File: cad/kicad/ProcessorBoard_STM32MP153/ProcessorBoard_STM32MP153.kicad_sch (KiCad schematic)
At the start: 4 parts

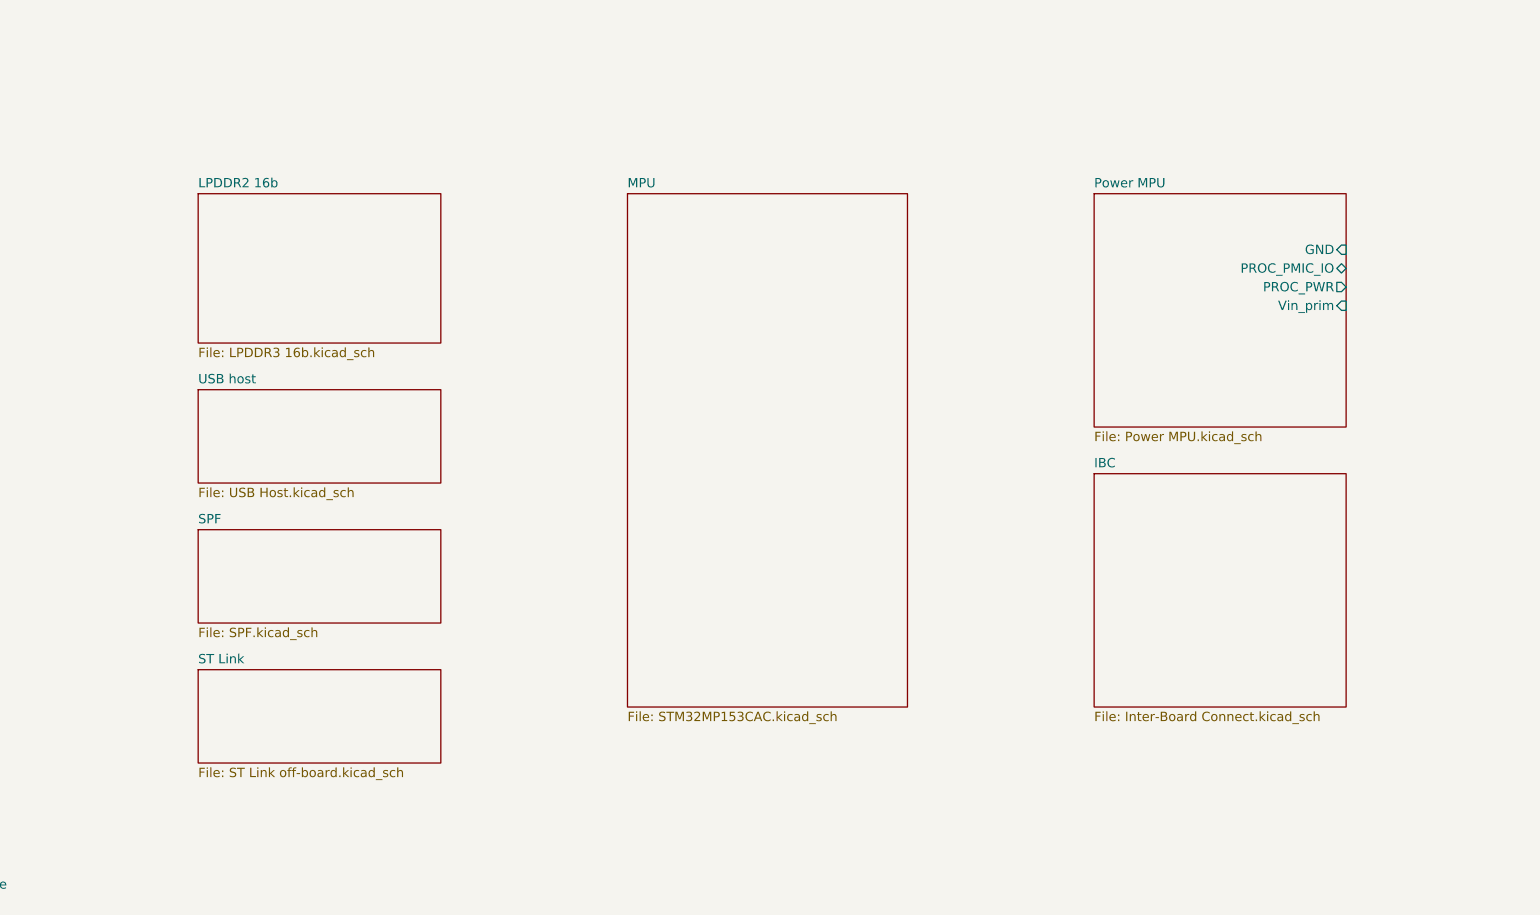
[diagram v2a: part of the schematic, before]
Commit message: verified jlc price category
~[32, 50]usd for 5 boards. includes impedence control. though must be 1oz top & bottom layers, 0.5oz inner layers . goes up at least $10usd for different pours
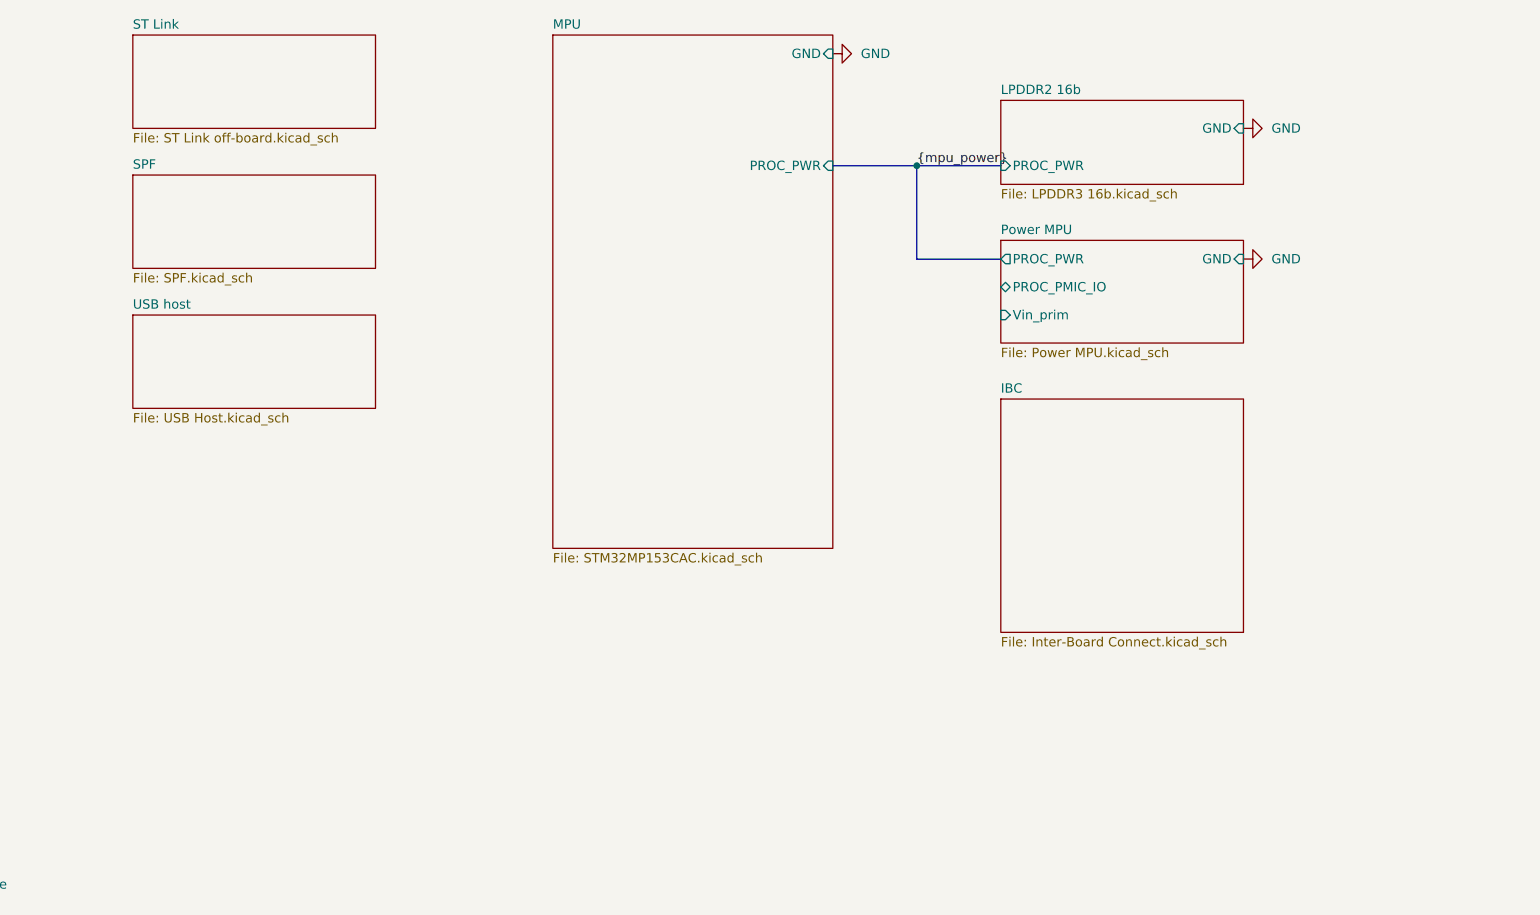
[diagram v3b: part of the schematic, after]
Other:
- sheet LPDDR2 16b ports: added GND, PROC_PWR; removed none
- sheet MPU ports: added GND, PROC_PWR; removed none

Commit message: mpu power connections
about mpu, apparently onboard usb supply has a requirement for the onboard ldo's to be happy, so u have to tap out 2 deticated pins. and theres also a power off sequence as well???
1v8 life looking better every day, 3v3(>2v9) trenches over there
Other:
- sheet LPDDR2 16b ports: added none; removed GND
- sheet MPU ports: added none; removed GND
- sheet Power MPU ports: added none; removed GND

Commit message: mr przudent get down
a thrid DDR voltage requirement has hit the power plane.
the cost of 11$ ram is apparently 3 distinct power nets :( .
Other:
- sheet LPDDR2 16b ports: added D_A_C; removed none
- sheet MPU ports: added MEM_D_A_C, PROC_PMIC_IO; removed none
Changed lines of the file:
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@@
+	(bus
+		(pts
+			(xy 154.94 66.04) (xy 177.8 66.04)
+		)
+		(stroke
+			(width 0)
+			(type default)
+		)
+	)
+	(bus
+		(pts
+			(xy 154.94 88.9) (xy 177.8 88.9)
+		)
+		(stroke
+			(width 0)
+			(type default)
+		)
+	)
 	(bus
 		(pts
@@
 	(label "{mpu_power}"
 		(at 166.37 72.39 0)
+		(effects
+			(font
+				(size 1.27 1.27)
+			)
+			(justify bottom)
+		)
+	)
+	(label "{mem_d_a_c}"
+		(at 166.37 66.04 0)
+		(effects
+			(font
+				(size 1.27 1.27)
+			)
+			(justify bottom)
+		)
+	)
+	(label "{mpu_pmic}"
+		(at 166.37 88.9 0)
 		(effects
 			(font
@@
 	)
 	(sheet
-		(at 116.84 54.61)
-		(size 38.1 69.85)
+		(at 116.84 63.5)
+		(size 38.1 60.96)
 		(exclude_from_sim no)
 		(in_bom yes)
@@
 		)
 		(property "Sheetname" "MPU"
-			(at 116.84 53.8984 0)
+			(at 116.84 62.7884 0)
 			(show_name no)
 			(do_not_autoplace no)
@@
 			)
 		)
+		(pin "PROC_PMIC_IO" bidirectional
+			(at 154.94 88.9 0)
+			(effects
+				(font
+					(size 1.27 1.27)
+				)
+				(justify right)
+			)
+		)
+		(pin "MEM_D_A_C" bidirectional
+			(at 154.94 66.04 0)
+			(effects
+				(font
+					(size 1.27 1.27)
+				)
+				(justify right)
+			)
+		)
 		(instances
 			(project "ProcessorBoard_STM32MP153"
@@
 	)
 	(sheet
-		(at 59.69 54.61)
+		(at 59.69 63.5)
 		(size 33.02 12.7)
 		(exclude_from_sim no)
@@
 		)
 		(property "Sheetname" "ST Link"
-			(at 59.69 53.8984 0)
+			(at 59.69 62.7884 0)
 			(show_name no)
 			(do_not_autoplace no)
@@
 		)
 		(property "Sheetfile" "ST Link off-board.kicad_sch"
-			(at 59.69 67.8946 0)
+			(at 59.69 76.7846 0)
 			(show_name no)
 			(do_not_autoplace no)
@@
 	)
 	(sheet
-		(at 59.69 73.66)
+		(at 59.69 82.55)
 		(size 33.02 12.7)
 		(exclude_from_sim no)
@@
 		)
 		(property "Sheetname" "SPF"
-			(at 59.69 72.9484 0)
+			(at 59.69 81.8384 0)
 			(show_name no)
 			(do_not_autoplace no)
@@
 		)
 		(property "Sheetfile" "SPF.kicad_sch"
-			(at 59.69 86.9446 0)
+			(at 59.69 95.8346 0)
 			(show_name no)
 			(do_not_autoplace no)
@@
 	)
 	(sheet
-		(at 59.69 92.71)
+		(at 59.69 101.6)
 		(size 33.02 12.7)
 		(exclude_from_sim no)
@@
 		)
 		(property "Sheetname" "USB host"
-			(at 59.69 91.9984 0)
+			(at 59.69 100.8884 0)
 			(show_name no)
 			(do_not_autoplace no)
@@
 		)
 		(property "Sheetfile" "USB Host.kicad_sch"
-			(at 59.69 105.9946 0)
+			(at 59.69 114.8846 0)
 			(show_name no)
 			(do_not_autoplace no)
@@
 			(effects
 				(font
+					(size 1.27 1.27)
+				)
+				(justify left)
+			)
+		)
+		(pin "D_A_C" bidirectional
+			(at 177.8 66.04 180)
+			(effects
+				(font

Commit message: is this tuff
most datasheets from LCSC are "not for public release"
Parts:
- H103: now not fitted
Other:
- note added: "replaced by keepout zone. to increase effective board space"
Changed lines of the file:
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@@
 		(comment 1 "fits in a Hammond 1593K Enclosure")
+	)
+	(text "replaced by keepout zone. to increase effective board space"
+		(exclude_from_sim no)
+		(at 44.958 179.07 0)
+		(effects
+			(font
+				(size 1.27 1.27)
+				(color 255 229 22 1)
+			)
+			(justify left top)
+		)
 	)
 	(junction
@@
 		(exclude_from_sim no)
 		(in_bom no)
-		(on_board yes)
-		(in_pos_files yes)
-		(dnp no)
+		(on_board no)
+		(in_pos_files no)
+		(dnp yes)
 		(fields_autoplaced yes)
 		(property "Reference" "H103"

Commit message: big ol kicad file ?
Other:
- added sheet Power SPF (Power SPF.kicad_sch)
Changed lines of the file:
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@@
 			(project "ProcessorBoard_STM32MP153"
 				(path "/e63e39d7-6ac0-4ffd-8aa3-1841a4541b55"
-					(page "9")
+					(page "999")
 				)
 			)
@@
 	)
 	(sheet
+		(at 59.69 101.6)
+		(size 33.02 12.7)
+		(exclude_from_sim no)
+		(in_bom yes)
+		(on_board yes)
+		(dnp no)
+		(fields_autoplaced yes)
+		(stroke
+			(width 0.1524)
+			(type solid)
+		)
+		(fill
+			(color 0 0 0 0)
+		)
+		(property "Sheetname" "Power SPF"
+			(at 59.69 100.8884 0)
+			(show_name no)
+			(do_not_autoplace no)
+			(effects
+				(font
+					(size 1.27 1.27)
+				)
+				(justify left bottom)
+			)
+		)
+		(property "Sheetfile" "Power SPF.kicad_sch"
+			(at 59.69 114.8846 0)
+			(show_name no)
+			(do_not_autoplace no)
+			(effects
+				(font
+					(size 1.27 1.27)
+				)
+				(justify left top)
+			)
+		)
+		(instances
+			(project "ProcessorBoard_STM32MP153"
+				(path "/e63e39d7-6ac0-4ffd-8aa3-1841a4541b55"
+					(page "6")
+				)
+			)
+		)
+	)
+	(sheet
 		(at 59.69 63.5)
 		(size 33.02 12.7)
@@
 			(project "ProcessorBoard_STM32MP153"
 				(path "/e63e39d7-6ac0-4ffd-8aa3-1841a4541b55"
-					(page "6")
+					(page "7")
 				)
 			)
@@
 	)
 	(sheet
-		(at 59.69 101.6)
+		(at 59.69 120.65)
 		(size 33.02 12.7)
 		(exclude_from_sim no)
@@
 		)
 		(property "Sheetname" "USB host"
-			(at 59.69 100.8884 0)
+			(at 59.69 119.9384 0)
 			(show_name no)
 			(do_not_autoplace no)
@@
 		)
 		(property "Sheetfile" "USB Host.kicad_sch"
-			(at 59.69 114.8846 0)
+			(at 59.69 133.9346 0)
 			(show_name no)
 			(do_not_autoplace no)
@@
 			(project "ProcessorBoard_STM32MP153"
 				(path "/e63e39d7-6ac0-4ffd-8aa3-1841a4541b55"
-					(page "7")
-				)
-			)
+					(page "9")
+				)
+			)

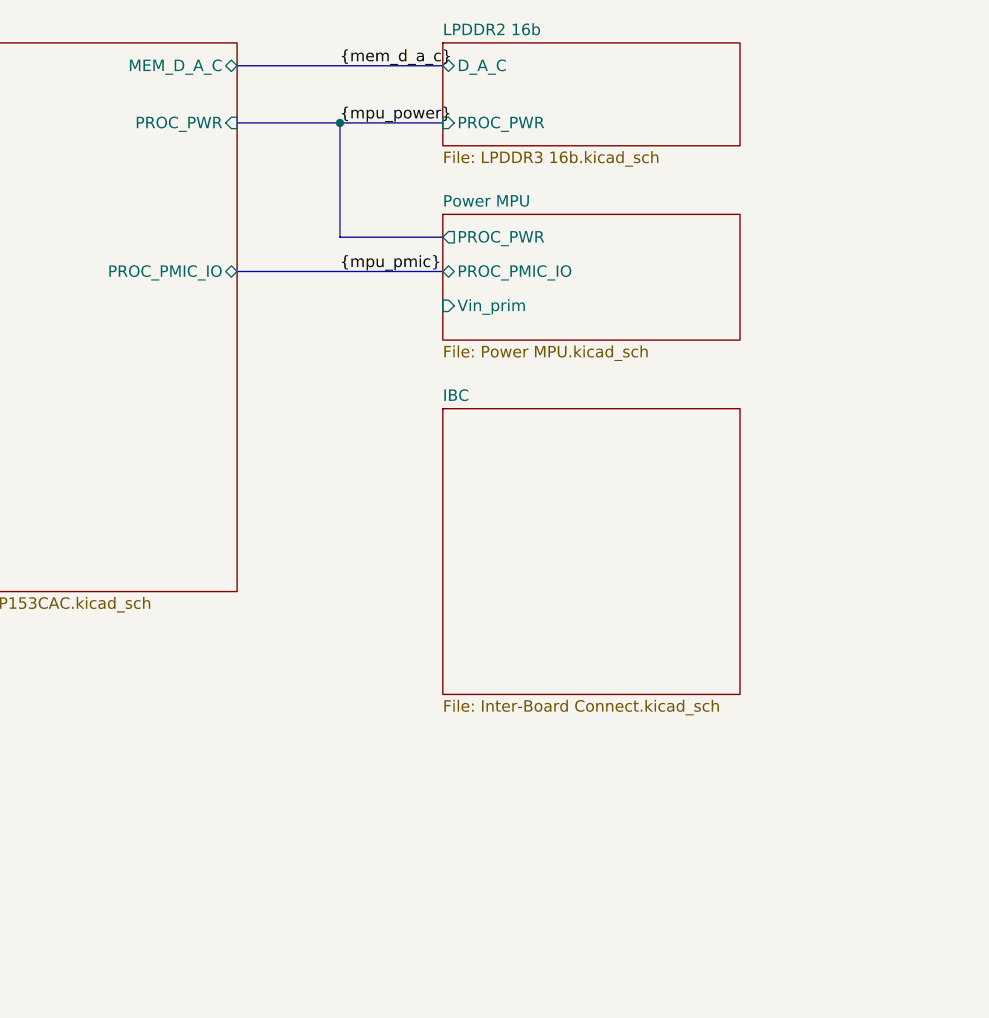
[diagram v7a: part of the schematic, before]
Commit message: new ram
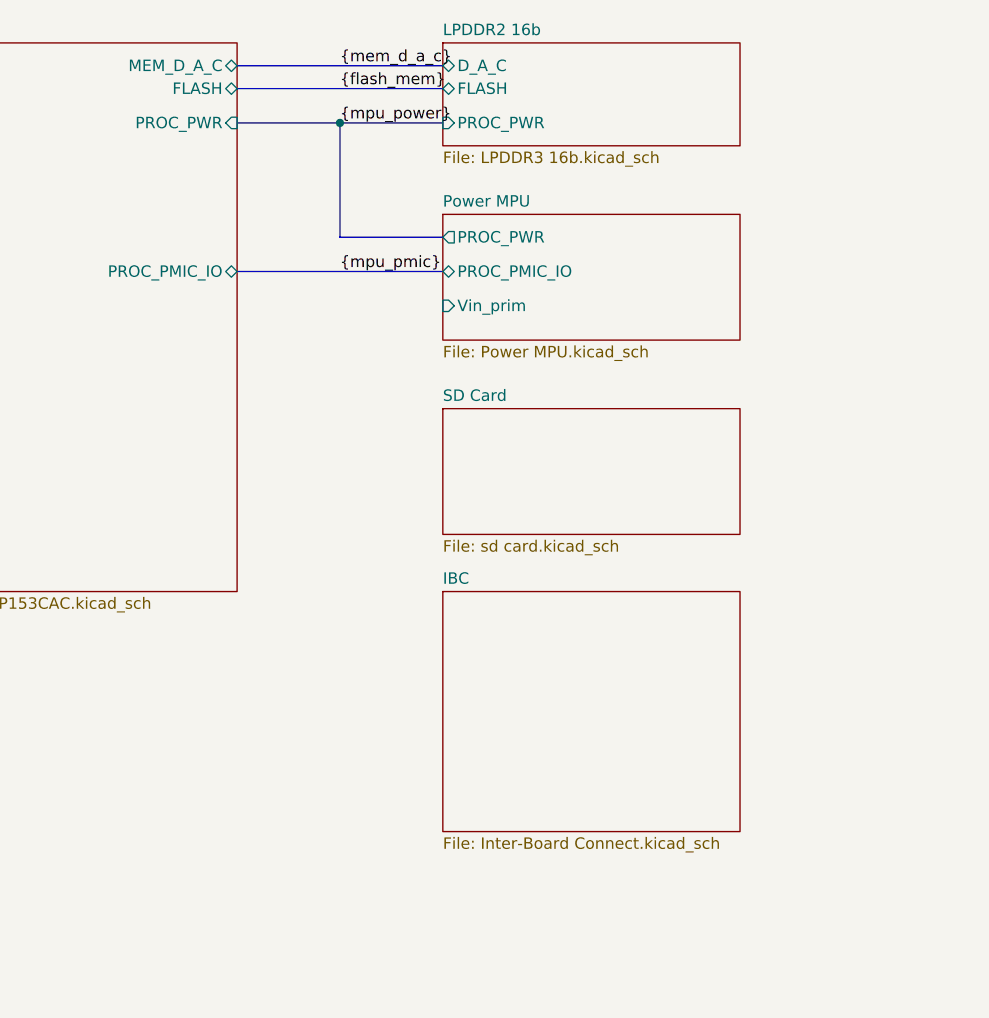
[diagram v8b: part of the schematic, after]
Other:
- added sheet SD Card (sd card.kicad_sch)
- sheet LPDDR2 16b ports: added FLASH; removed none
- sheet MPU ports: added FLASH; removed none
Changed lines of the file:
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@@
+	(bus
+		(pts
+			(xy 154.94 68.58) (xy 177.8 68.58)
+		)
+		(stroke
+			(width 0)
+			(type default)
+		)
+	)
 	(bus
 		(pts
@@
 	(label "{mem_d_a_c}"
 		(at 166.37 66.04 0)
+		(effects
+			(font
+				(size 1.27 1.27)
+			)
+			(justify bottom)
+		)
+	)
+	(label "{flash_mem}"
+		(at 166.37 68.58 0)
 		(effects
 			(font
@@
 			)
 		)
+		(pin "FLASH" bidirectional
+			(at 154.94 68.58 0)
+			(effects
+				(font
+					(size 1.27 1.27)
+				)
+				(justify right)
+			)
+		)
 		(instances
 			(project "ProcessorBoard_STM32MP153"
@@
 	)
 	(sheet
+		(at 177.8 104.14)
+		(size 33.02 13.97)
+		(exclude_from_sim no)
+		(in_bom yes)
+		(on_board yes)
+		(dnp no)
+		(fields_autoplaced yes)
+		(stroke
+			(width 0.1524)
+			(type solid)
+		)
+		(fill
+			(color 0 0 0 0)
+		)
+		(property "Sheetname" "SD Card"
+			(at 177.8 103.4284 0)
+			(show_name no)
+			(do_not_autoplace no)
+			(effects
+				(font
+					(size 1.27 1.27)
+				)
+				(justify left bottom)
+			)
+		)
+		(property "Sheetfile" "sd card.kicad_sch"
+			(at 177.8 118.6946 0)
+			(show_name no)
+			(do_not_autoplace no)
+			(effects
+				(font
+					(size 1.27 1.27)
+				)
+				(justify left top)
+			)
+		)
+		(instances
+			(project "ProcessorBoard_STM32MP153"
+				(path "/e63e39d7-6ac0-4ffd-8aa3-1841a4541b55"
+					(page "10")
+				)
+			)
+		)
+	)
+	(sheet
 		(at 59.69 63.5)
 		(size 33.02 12.7)
@@
 	)
 	(sheet
-		(at 177.8 104.14)
-		(size 33.02 31.75)
+		(at 177.8 124.46)
+		(size 33.02 26.67)
 		(exclude_from_sim no)
 		(in_bom yes)
@@
 		)
 		(property "Sheetname" "IBC"
-			(at 177.8 103.4284 0)
+			(at 177.8 123.7484 0)
 			(show_name no)
 			(do_not_autoplace no)
@@
 		)
 		(property "Sheetfile" "Inter-Board Connect.kicad_sch"
-			(at 177.8 136.4746 0)
+			(at 177.8 151.7146 0)
 			(show_name no)
 			(do_not_autoplace no)
@@
 			(effects
 				(font
+					(size 1.27 1.27)
+				)
+				(justify left)
+			)
+		)
+		(pin "FLASH" bidirectional
+			(at 177.8 68.58 180)
+			(effects
+				(font
